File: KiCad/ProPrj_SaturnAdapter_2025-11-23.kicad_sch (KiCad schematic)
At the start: 30 parts, among them Q1 BSS138B, Q2 BSS138B, Q3 BSS138B, Q4 BSS138B, Q5 BSS138B, Q6 BSS138B, Q7 BSS138B, SW1 MINI MSK12CO2, U3 RP2040-Zero, U4 D-SUB-DR-9PCM-CB

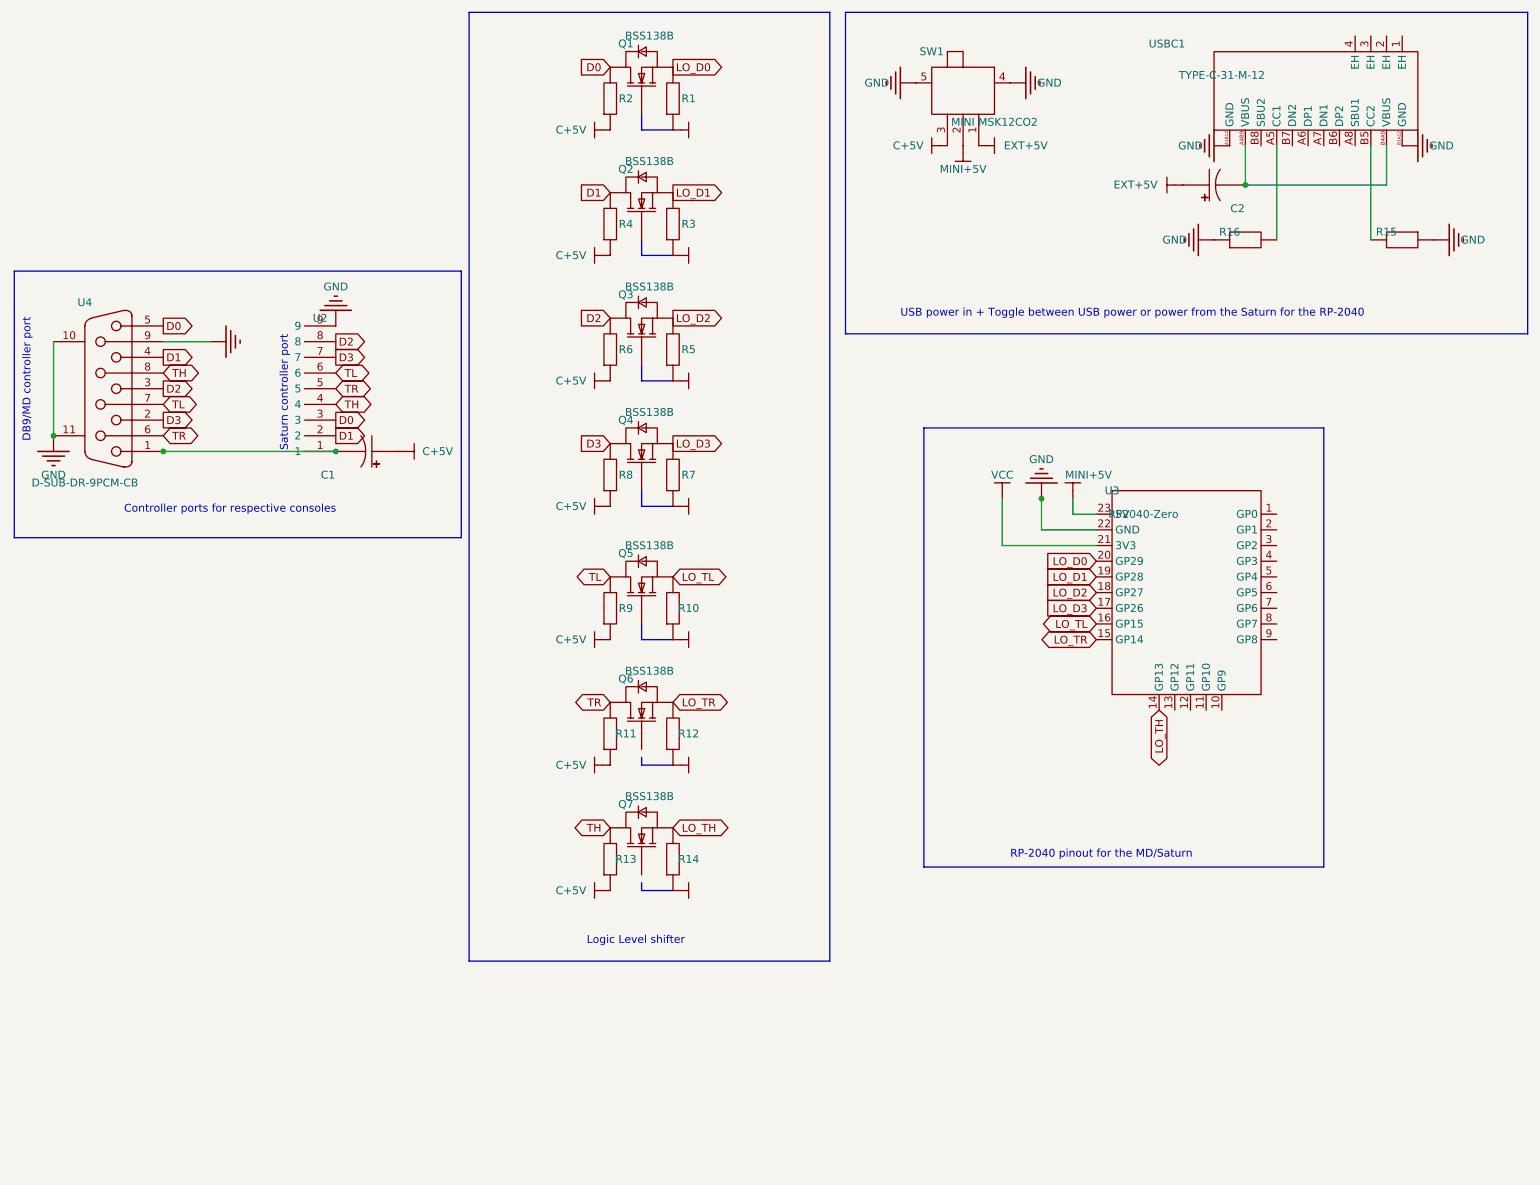
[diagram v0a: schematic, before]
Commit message: Updated schematic for neatness, and further shrank the PCB with the USB-C port brought closer to center
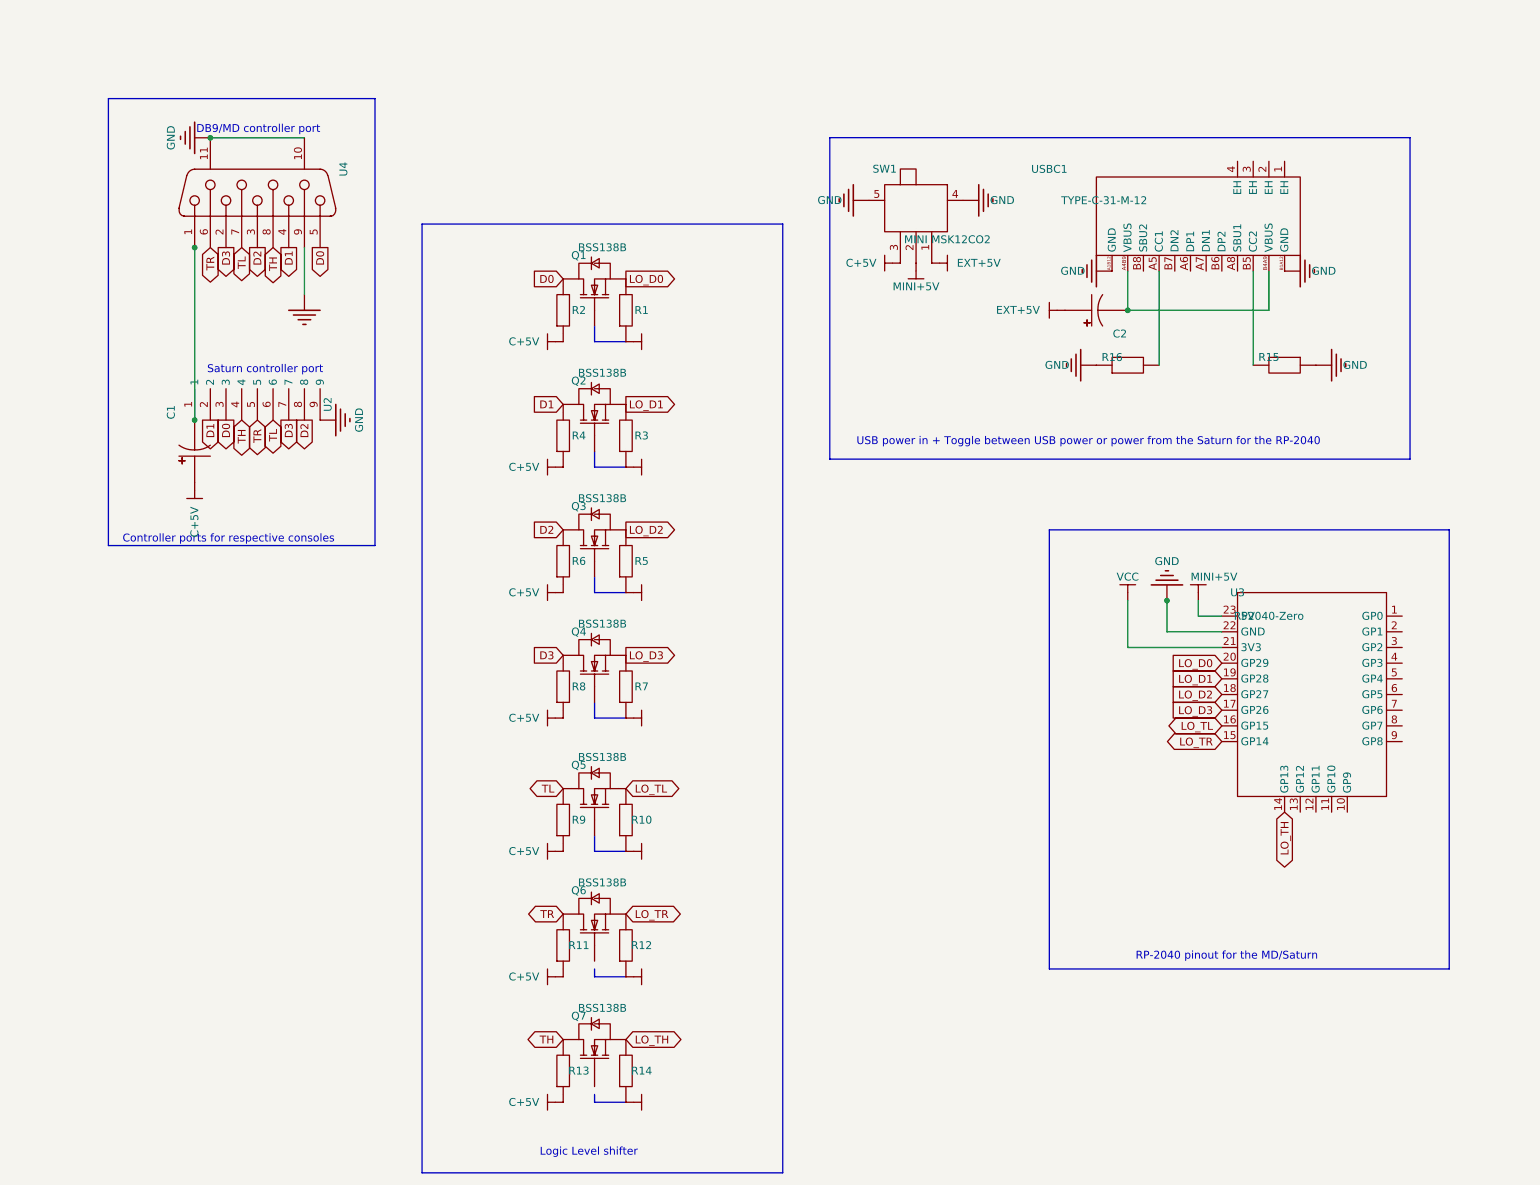
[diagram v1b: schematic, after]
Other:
- moved on the sheet: C1, C2, Q1, Q2, Q3, Q4, Q5, Q6, Q7, R1, R10, R11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

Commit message: Fix capacitors (Had it in line with the 5v rail rather than properly smoothing [facepalm ]
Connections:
- net C+5V: now also U4.1
- net EXT+5V: now also USBC1.A4B9 (VBUS), USBC1.B4A9 (VBUS)
- net at U4.9: now also C1.2
- now unconnected: C2.2, U2.1
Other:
- moved on the sheet: C1, C2, R16

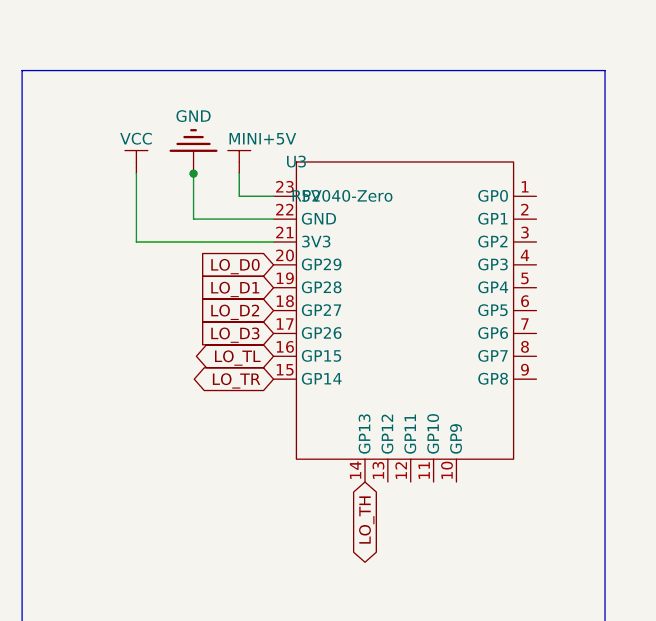
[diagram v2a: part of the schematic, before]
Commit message: Edits to files to facilitate prototype production, incl. gerbers.
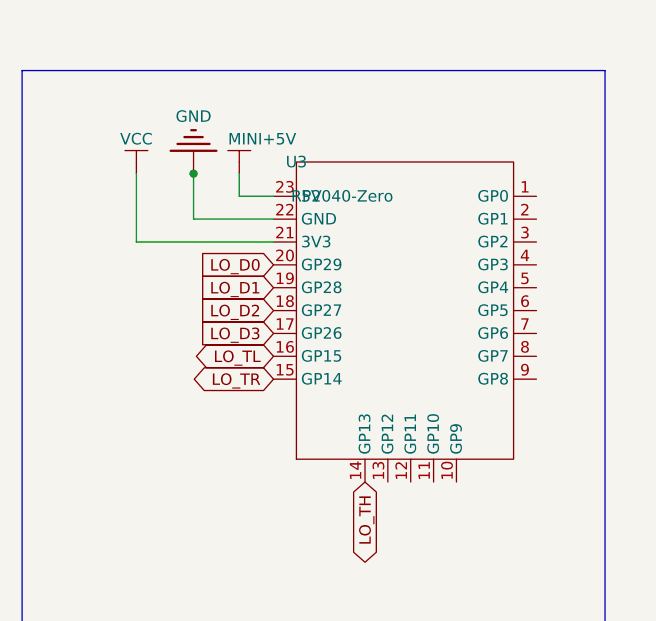
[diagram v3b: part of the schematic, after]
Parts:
- C1, C2: MPN (none) -> C122260
- Q1, Q2, Q3, Q4, Q5, Q6, Q7: MPN (none) -> C20599939
- R15, R16: MPN (none) -> C2907044
- SW1: MPN (none) -> C2681570
- U3: footprint ProPrj_Sat-easyedapro:COMM-SMD_RP2040-ZERO -> ProPrj_Sat-easyedapro:RP2040-ZERO DIP
- U4: MPN (none) -> C19077337
- USBC1: MPN (none) -> C165948
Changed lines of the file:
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@@
 			)
 		)
+		(property "MPN" "C122260"
+			(at 180.34 53.34 0)
+			(effects
+				(font
+					(size 1.27 1.27)
+				)
+				(hide yes)
+			)
+		)
 		(pin "2"
 		)
@@
 			)
 		)
+		(property "MPN" "C2907044"
+			(at 205.74 57.15 0)
+			(effects
+				(font
+					(size 1.27 1.27)
+				)
+				(hide yes)
+			)
+		)
 		(pin "2"
 		)
@@
 			)
 		)
+		(property "MPN" "C122260"
+			(at 38.1 48.26 0)
+			(effects
+				(font
+					(size 1.27 1.27)
+				)
+				(hide yes)
+			)
+		)
 		(pin "1"
 		)
@@
 			)
 		)
-		(property "Footprint" "ProPrj_Sat-easyedapro:COMM-SMD_RP2040-ZERO"
+		(property "Footprint" "ProPrj_Sat-easyedapro:RP2040-ZERO DIP"
 			(at 210.82 111.76 0)
 			(effects
@@
 			)
 		)
-		(property "Datasheet" "https://item.szlcsc.com/datasheet/RP2040-Zero/6136910.html"
+		(property "Datasheet" "https://atta.szlcsc.com/upload/public/pdf/source/20230328/F7ADB41143C3623278858A7E8047DBCD.pdf"
 			(at 210.82 111.76 0)
 			(effects
@@
 			)
 		)
+		(property "MPN" "C20599939"
+			(at 93.98 106.68 0)
+			(effects
+				(font
+					(size 1.27 1.27)
+				)
+				(hide yes)
+			)
+		)
 		(pin "1"
 		)
@@
 			)
 		)
+		(property "MPN" "C2907044"
+			(at 205.74 62.23 0)
+			(effects
+				(font
+					(size 1.27 1.27)
+				)
+				(hide yes)
+			)
+		)
 		(pin "2"
 		)
@@
 			)
 		)
+		(property "MPN" "C20599939"
+			(at 93.98 66.04 0)
+			(effects
+				(font
+					(size 1.27 1.27)
+				)
+				(hide yes)
+			)
+		)
 		(pin "1"
 		)
@@
 			)
 		)
+		(property "MPN" "C20599939"
+			(at 93.98 128.27 0)
+			(effects
+				(font
+					(size 1.27 1.27)
+				)
+				(hide yes)
+			)
+		)
 		(pin "1"
 		)
@@
 			)
 		)
+		(property "MPN" "C20599939"
+			(at 93.98 168.91 0)
+			(effects
+				(font
+					(size 1.27 1.27)
+				)
+				(hide yes)
+			)
+		)
 		(pin "1"
 		)
@@
 			)
 		)
+		(property "MPN" "C2681570"
+			(at 146.05 32.9946 0)
+			(effects
+				(font
+					(size 1.27 1.27)
+				)
+				(hide yes)
+			)
+		)
 		(pin "4"
 		)
@@
 			)
 		)
+		(property "MPN" "C19077337"
+			(at 39.37 27.94 0)
+			(effects
+				(font
+					(size 1.27 1.27)
+				)
+				(hide yes)
+			)
+		)
 		(pin "1"
 		)
@@
 			)
 		)
+		(property "MPN" "C20599939"
+			(at 93.98 86.36 0)
+			(effects
+				(font
+					(size 1.27 1.27)
+				)
+				(hide yes)
+			)
+		)
 		(pin "1"
 		)
@@
 			)
 		)
+		(property "MPN" "C20599939"
+			(at 93.98 148.59 0)
+			(effects
+				(font
+					(size 1.27 1.27)
+				)
+				(hide yes)
+			)
+		)
 		(pin "1"
 		)
@@
 			)
 		)
+		(property "MPN" "C165948"
+			(at 191.77 33.02 0)
+			(effects
+				(font
+					(size 1.27 1.27)
+				)
+				(hide yes)
+			)
+		)
 		(pin "A1B12"
 		)
@@
 			(at 93.98 45.72 0)
 			(effects
+				(font
+					(size 1.27 1.27)
+				)
+				(hide yes)
+			)
+		)
+		(property "MPN" "C20599939"
+			(at 93.98 45.72 0)
+			(effects

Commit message: Price optimisation by changing of certain components from the Extended LCSC set to the JLCPCB Basic set + minor changes
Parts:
- removed C1, C2: 10uF, ProPrj_Sat-easyedapro:CASE-A_3216, symbol ProPrj_Sat-easyedapro:T491A106K006AT
- removed R1, R10, R11, R12, R13, R14, R2, R3, R4, R5, R6, R7, R8, R9: 10K, ProPrj_Sat-easyedapro:R0603, symbol ProPrj_Sat-easyedapro:Res
- removed R15, R16: 5.1kΩ, ProPrj_Sat-easyedapro:R0603, symbol ProPrj_Sat-easyedapro:FRC0603F5101TS
- added C1, C2: 10uF, C_1206_3216Metric_Pad1.33x1.80mm_HandSolder, symbol Device:C_Polarized_Small_US
- added R1, R10, R11, R12, R13, R14, R2, R3, R4, R5, R6, R7, R8, R9: 10k, R0603, symbol Device:R
- added R15, R16: 5.1k, R0603, symbol Device:R
- U2: value (none) -> ~
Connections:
- net C+5V: now also U2.1, C2.1, R10.2, R12.2, R14.2, R2.2, R4.1, R6.2, R8.2; no longer SW1.3
- net D0: now also R2.1
- net D1: now also R4.2
- net D2: now also R6.1
- net D3: now also R8.1
- net GND: now also U4.9, C1.2, C2.2, R15.1, R16.1; no longer SW1.4, SW1.5, USBC1.A1B12 (GND), USBC1.B1A12 (GND)
- net LO_D0: now also R1.1
- net LO_D1: now also R3.2
- net LO_D2: now also R5.1
- net LO_D3: now also R7.1
- net LO_TH: now also R13.1
- net LO_TL: now also R9.1
- net LO_TR: now also R11.1
- net MINI+5V: no longer SW1.2
- net TH: now also R14.1
- net TL: now also R10.1
- net TR: now also R12.1
- net VCC: now also Q1.1 (G), Q2.1 (G), Q3.1 (G), Q4.1 (G), Q5.1 (G), Q6.1 (G), Q7.1 (G), R1.2, R11.2, R13.2, R3.1, R5.2, R7.2, R9.2
- net at USBC1.A5 (CC1): now also R16.2
- net at USBC1.B5 (CC2): now also R15.2
- net EXT+5V renamed EXT5V
- net EXT5V: now also C1.1; no longer SW1.1
- no-connect marks 0 -> 8
